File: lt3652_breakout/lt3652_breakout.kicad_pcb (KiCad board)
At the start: 2 copper layers, 45.2 x 33 mm, 15 parts, among them CON1 SLR PNL, P3 GND, U1 LT3652

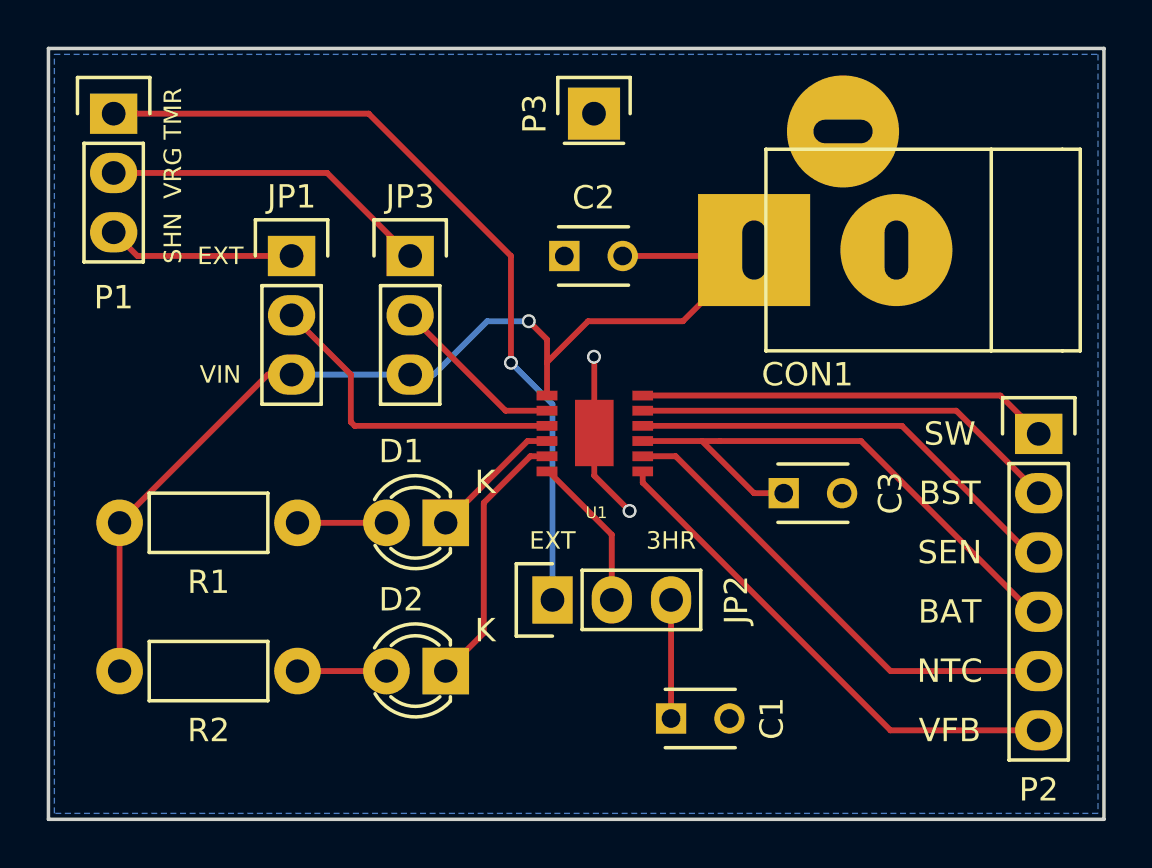
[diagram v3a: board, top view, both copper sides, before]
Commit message: Started work on Rev 0.2, with the aim of using trimmer to configure the LT3652
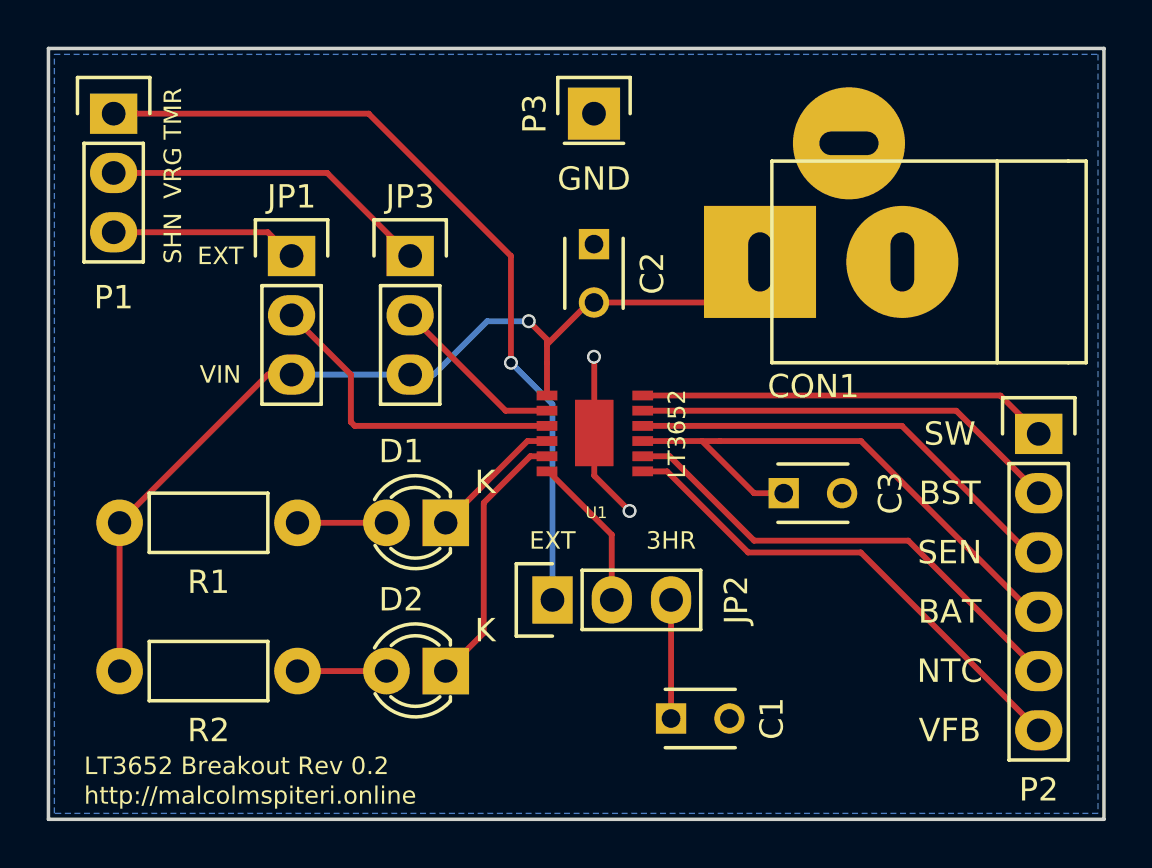
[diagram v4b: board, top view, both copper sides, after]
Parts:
- moved C2 1.37 mm to (147.3, 99.8), turned to 270 degrees
- moved CON1 0.57 mm to (160.5, 100.6)
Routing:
- net VIN: track 48.6 -> 45.1 mm
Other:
- board text added: "GND"
- board text added: "LT3652"
- board text added: "LT3652 Breakout Rev 0.2"
- board text added: "http://malcolmspiteri.online"
- board text removed: "Crappy LT3652 Breakout Board Rev 0.1 malcolmspiterionline@gmail.com"
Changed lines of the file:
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@@
     (area 123.876999 91.364999 169.239001 124.535001)
     (thickness 1.6)
-    (drawings 18)
-    (tracks 73)
+    (drawings 21)
+    (tracks 77)
     (zones 0)
     (modules 15)
@@
     (title "Crappy LT3652 Breakout")
     (date 2016-02-16)
-    (rev 0.1)
+    (rev 0.2)
     (company "Malcolm Spiteri")
   )
@@
     (aux_axis_origin 0 0)
     (grid_origin 147.066 107.95)
-    (visible_elements 7FFCFFFF)
+    (visible_elements 7FFFFFFF)
     (pcbplotparams
       (layerselection 0x010f0_80000001)
@@
   )
   (module Connect:JACK_ALIM (layer F.Cu)
-    (at 160.274 100.076 180)
+    (at 160.528 100.584 180)
     (descr "module 1 pin (ou trou mecanique de percage)")
     (tags "CONN JACK")
@@
   )
   (module Capacitors_ThroughHole:C_Disc_D3_P2.5 (layer F.Cu)
-    (at 146.05 100.33)
+    (at 147.32 99.822 270)
     (descr "Capacitor 3mm Disc, Pitch 2.5mm")
     (tags Capacitor)
-    (fp_text reference C2 (at 1.25 -2.5) (layer F.SilkS)
-      (effects (font (size 1 1) (thickness 0.15)))
-    )
-    (fp_text value 10uF (at 1.25 2.5) (layer F.Fab)
+    (fp_text reference C2 (at 1.25 -2.5 270) (layer F.SilkS)
+      (effects (font (size 1 1) (thickness 0.15)))
+    )
+    (fp_text value 10uF (at 1.25 2.5 270) (layer F.Fab)
       (effects (font (size 1 1) (thickness 0.15)))
     )
@@
     (fp_line (start -0.25 -1.25) (end 2.75 -1.25) (layer F.SilkS) (width 0.15))
     (fp_line (start 2.75 1.25) (end -0.25 1.25) (layer F.SilkS) (width 0.15))
-    (pad 1 thru_hole rect (at 0 0) (size 1.3 1.3) (drill 0.8) (layers *.Cu *.Mask F.SilkS)
+    (pad 1 thru_hole rect (at 0 0 270) (size 1.3 1.3) (drill 0.8) (layers *.Cu *.Mask F.SilkS)
       (net 13 GND))
-    (pad 2 thru_hole circle (at 2.5 0) (size 1.3 1.3) (drill 0.8001) (layers *.Cu *.Mask F.SilkS)
+    (pad 2 thru_hole circle (at 2.5 0 270) (size 1.3 1.3) (drill 0.8001) (layers *.Cu *.Mask F.SilkS)
       (net 7 VIN))
     (model Capacitors_ThroughHole.3dshapes/C_Disc_D3_P2.5.wrl
@@
     )
   )
+  (gr_text GND (at 147.32 97.028) (layer F.SilkS)
+    (effects (font (size 1 1) (thickness 0.2)))
+  )
+  (gr_text http://malcolmspiteri.online (at 125.476 123.444) (layer F.SilkS)
+    (effects (font (size 0.75 0.75) (thickness 0.15)) (justify left))
+  )
+  (gr_text "LT3652 Breakout Rev 0.2" (at 125.476 122.174) (layer F.SilkS)
+    (effects (font (size 0.75 0.75) (thickness 0.15)) (justify left))
+  )
+  (gr_text LT3652 (at 150.876 107.95 90) (layer F.SilkS)
+    (effects (font (size 0.75 0.75) (thickness 0.15)))
+  )
   (gr_text SHN (at 129.286 99.568 90) (layer F.SilkS)
     (effects (font (size 0.75 0.75) (thickness 0.15)))
@@
   (gr_text TMR (at 129.286 94.234 90) (layer F.SilkS)
     (effects (font (size 0.75 0.75) (thickness 0.15)))
-  )
-  (gr_text "Crappy LT3652 Breakout Board\nRev 0.1\nmalcolmspiterionline@gmail.com" (at 163.576 119.38) (layer B.SilkS)
-    (effects (font (size 1.5 1.5) (thickness 0.3)) (justify left mirror))
   )
   (gr_text VIN (at 131.318 105.41) (layer F.SilkS)
@@
   (segment (start 144.5925 108.9075) (end 142.6 110.9) (width 0.25) (layer F.Cu) (net 3))
   (segment (start 134.62 118.11) (end 138.43 118.11) (width 0.25) (layer F.Cu) (net 4))
-  (segment (start 134.366 100.33) (end 127.762 100.33) (width 0.25) (layer F.Cu) (net 5) (status 10))
-  (segment (start 127.762 100.33) (end 126.746 99.314) (width 0.25) (layer F.Cu) (net 5))
+  (segment (start 126.746 99.314) (end 133.35 99.314) (width 0.25) (layer F.Cu) (net 5) (status 400000))
+  (segment (start 133.35 99.314) (end 134.366 100.33) (width 0.25) (layer F.Cu) (net 5) (status 800000))
   (segment (start 145.3075 106.9575) (end 143.5335 106.9575) (width 0.25) (layer F.Cu) (net 6))
   (segment (start 143.5335 106.9575) (end 139.446 102.87) (width 0.25) (layer F.Cu) (net 6))
+  (segment (start 147.32 102.322) (end 152.694 102.322) (width 0.25) (layer F.Cu) (net 7) (status C00000))
+  (segment (start 152.694 102.322) (end 154.432 100.584) (width 0.25) (layer F.Cu) (net 7) (status C00000))
+  (segment (start 147.32 102.322) (end 147.106 102.322) (width 0.25) (layer F.Cu) (net 7) (status C00000))
+  (segment (start 147.106 102.322) (end 145.3075 104.1205) (width 0.25) (layer F.Cu) (net 7) (status 400000))
+  (segment (start 153.162 101.854) (end 154.432 100.584) (width 0.25) (layer F.Cu) (net 7))
+  (segment (start 154.178 100.33) (end 154.432 100.584) (width 0.25) (layer F.Cu) (net 7))
   (segment (start 127 118.11) (end 127 111.76) (width 0.25) (layer F.Cu) (net 7))
   (segment (start 134.366 105.41) (end 133.35 105.41) (width 0.25) (layer F.Cu) (net 7))
@@
   (segment (start 139.446 105.41) (end 140.462 105.41) (width 0.25) (layer B.Cu) (net 7))
   (segment (start 140.462 105.41) (end 142.748 103.124) (width 0.25) (layer B.Cu) (net 7))
-  (segment (start 145.3075 103.9055) (end 145.3075 104.902) (width 0.25) (layer F.Cu) (net 7))
+  (segment (start 145.3075 103.9055) (end 145.3075 104.1205) (width 0.25) (layer F.Cu) (net 7))
+  (segment (start 145.3075 104.1205) (end 145.3075 104.902) (width 0.25) (layer F.Cu) (net 7))
   (segment (start 144.526 103.124) (end 145.3075 103.9055) (width 0.25) (layer F.Cu) (net 7))
   (via (at 144.526 103.124) (size 0.6) (drill 0.4) (layers F.Cu B.Cu) (net 7))
@@
   (segment (start 127 111.76) (end 127 110.998) (width 0.25) (layer F.Cu) (net 7))
   (segment (start 134.366 105.41) (end 139.446 105.41) (width 0.25) (layer B.Cu) (net 7) (status 10))
-  (segment (start 148.55 100.33) (end 153.924 100.33) (width 0.25) (layer F.Cu) (net 7))
-  (segment (start 153.924 100.33) (end 154.178 100.076) (width 0.25) (layer F.Cu) (net 7))
+  (segment (start 154.178 100.838) (end 154.432 100.584) (width 0.25) (layer F.Cu) (net 7) (status 30))
   (segment (start 145.3075 106.3075) (end 145.3075 104.902) (width 0.25) (layer F.Cu) (net 7))
-  (segment (start 145.3075 104.902) (end 145.3075 104.8825) (width 0.25) (layer F.Cu) (net 7))
-  (segment (start 151.13 103.124) (end 154.178 100.076) (width 0.25) (layer F.Cu) (net 7))
-  (segment (start 147.066 103.124) (end 151.13 103.124) (width 0.25) (layer F.Cu) (net 7))
-  (segment (start 145.3075 104.8825) (end 147.066 103.124) (width 0.25) (layer F.Cu) (net 7))
-  (segment (start 153.924 100.33) (end 153.924 100.05568) (width 0.25) (layer F.Cu) (net 7))
+  (segment (start 154.178 100.838) (end 154.178 100.56368) (width 0.25) (layer F.Cu) (net 7) (status 30))
   (segment (start 126.746 94.234) (end 137.668 94.234) (width 0.25) (layer F.Cu) (net 8))
   (segment (start 145.542 106.68) (end 145.542 115.062) (width 0.25) (layer B.Cu) (net 8))
@@
   (segment (start 165.93 113.03) (end 160.5075 107.6075) (width 0.25) (layer F.Cu) (net 18))
   (segment (start 160.5075 107.6075) (end 149.4075 107.6075) (width 0.25) (layer F.Cu) (net 18))
-  (segment (start 149.4075 108.9075) (end 150.8175 108.9075) (width 0.25) (layer F.Cu) (net 19))
-  (segment (start 160.02 118.11) (end 166.37 118.11) (width 0.25) (layer F.Cu) (net 19))
-  (segment (start 150.8175 108.9075) (end 160.02 118.11) (width 0.25) (layer F.Cu) (net 19))
-  (segment (start 149.4075 109.5575) (end 149.4075 110.0375) (width 0.25) (layer F.Cu) (net 20))
-  (segment (start 160.02 120.65) (end 166.37 120.65) (width 0.25) (layer F.Cu) (net 20))
-  (segment (start 149.4075 110.0375) (end 160.02 120.65) (width 0.25) (layer F.Cu) (net 20))
+  (segment (start 149.4075 108.9075) (end 150.5635 108.9075) (width 0.25) (layer F.Cu) (net 19))
+  (segment (start 160.782 112.522) (end 166.37 118.11) (width 0.25) (layer F.Cu) (net 19))
+  (segment (start 154.178 112.522) (end 160.782 112.522) (width 0.25) (layer F.Cu) (net 19))
+  (segment (start 150.5635 108.9075) (end 154.178 112.522) (width 0.25) (layer F.Cu) (net 19))
+  (segment (start 149.4075 109.5575) (end 150.4515 109.5575) (width 0.25) (layer F.Cu) (net 20))
+  (segment (start 158.75 113.03) (end 166.37 120.65) (width 0.25) (layer F.Cu) (net 20))
+  (segment (start 153.924 113.03) (end 158.75 113.03) (width 0.25) (layer F.Cu) (net 20))
+  (segment (start 150.4515 109.5575) (end 153.924 113.03) (width 0.25) (layer F.Cu) (net 20))
   (zone (net 13) (net_name GND) (layer B.Cu) (hatch edge 0.508)
     (connect_pads (clearance 0.508))

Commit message: WIP on Rev 0.2
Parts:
- removed JP1: SHDN OPT, Pin_Headers:Pin_Header_Straight_1x03
- removed JP3: VREG OPT, Pin_Headers:Pin_Header_Straight_1x03
- removed P2: , Pin_Headers:Pin_Header_Straight_1x06
- removed P3: GND, Pin_Headers:Pin_Header_Straight_1x01
- added RV1: POT, bourns_trim_pots:Bourns_3362P_Trimmer, F.Cu at (166.1, 120.8)
- added RV2: POT, bourns_trim_pots:Bourns_3362P_Trimmer, F.Cu at (166.1, 113.8)
- added W1: TEST_1P, pcb_test_points:KEYSTONE_5016_PCB_Test_Point, F.Cu at (177.1, 114.5)
- added W2: TEST_1P, pcb_test_points:KEYSTONE_5016_PCB_Test_Point, F.Cu at (177.0, 120.5)
- C1, C2, C3: footprint Capacitors_ThroughHole:C_Disc_D3_P2.5 -> Capacitors_SMD:C_0603_HandSoldering
- D1: value (none) -> 3mm GRN; footprint LEDs:LED-3MM -> LEDs:LED_0603
- D2: value (none) -> 3mm RED; footprint LEDs:LED-3MM -> LEDs:LED_0603
- P1: value (none) -> CONN_01X09; footprint Pin_Headers:Pin_Header_Straight_1x03 -> Pin_Headers:Pin_Header_Straight_1x09
- R1, R2: footprint Resistors_ThroughHole:Resistor_Horizontal_RM7mm -> Resistors_SMD:R_0603_HandSoldering
- moved P1 52.4 mm to (167.9, 126.7), turned to 270 degrees
- moved C2 17.3 mm to (160.4, 111.2), turned to 180 degrees
- moved R2 15.7 mm to (147.3, 108.8), turned to 90 degrees
- moved R1 15.0 mm to (149.3, 108.8), turned to 90 degrees
- moved U1 13.2 mm to (157.9, 116.0), turned to 270 degrees
- moved D2 13.1 mm to (152.7, 112.2)
- moved D1 11.8 mm to (152.7, 110.0)
- moved C3 10.9 mm to (157.6, 121.2), turned to 270 degrees
- moved JP2 8.14 mm to (147.6, 123.0), turned to 180 degrees
- moved C1 6.41 mm to (147.7, 114.5)
- moved CON1 5.17 mm to (161.6, 105.7)
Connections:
- C2 pad 2: VIN -> /VIN
- CON1 pad 1: VIN -> /VIN
- CON1 pad 3: Net-(CON1-Pad3) -> (no net)
- P1 pad 1: Net-(JP2-Pad1) -> /VIN
- P1 pad 2: Net-(JP3-Pad1) -> Net-(P1-Pad2)
- P1 pad 3: Net-(JP1-Pad1) -> Net-(P1-Pad3)
- R1 pad 2: VIN -> /VIN
- R2 pad 2: VIN -> /VIN
- U1 pad 1: VIN -> /VIN
- U1 pad 10: Net-(P2-Pad3) -> Net-(P1-Pad4)
- U1 pad 11: Net-(P2-Pad2) -> Net-(P1-Pad3)
- U1 pad 12: Net-(P2-Pad1) -> Net-(P1-Pad2)
- U1 pad 2: VREG -> /VIN_REG
- U1 pad 3: SHDN -> /SHDN
- U1 pad 7: Net-(P2-Pad6) -> Net-(P1-Pad7)
- U1 pad 8: Net-(P2-Pad5) -> Net-(P1-Pad6)
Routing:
- net VIN: track 45.1 -> 0.00 mm, vias 1 -> 0
- net /VIN: track 0.00 -> 42.7 mm, vias 0 -> 2
- net Net-(JP2-Pad1): track 35.0 -> 4.74 mm, vias 1 -> 0
- net Net-(P2-Pad6): track 21.6 -> 0.00 mm
- net Net-(P2-Pad5): track 20.8 -> 0.00 mm
- net Net-(P2-Pad3): track 19.2 -> 0.00 mm
- net Net-(P2-Pad2): track 18.4 -> 0.00 mm
- net Net-(P2-Pad1): track 17.6 -> 0.00 mm
- net /VIN_REG: track 0.00 -> 16.2 mm
- net Net-(C3-Pad1): track 24.4 -> 9.75 mm
- net Net-(JP3-Pad1): track 14.2 -> 0.00 mm
- net SHDN: track 14.1 -> 0.00 mm
- net /SHDN: track 0.00 -> 12.1 mm
- net Net-(P1-Pad2): track 0.00 -> 11.0 mm
- net Net-(P1-Pad3): track 0.00 -> 10.2 mm
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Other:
- board size 45.2 x 33 mm -> 24.2 x 32.2 mm
- board text added: "BOOST"
- board text removed: "BAT"
- board text removed: "BST"
- board text removed: "LT3652"
- board text removed: "NTC"
- board text removed: "SEN"
- board text removed: "SHN"
- board text removed: "TMR"
- board text removed: "VFB"
- board text removed: "VRG"
- board text removed: "http://malcolmspiteri.online"

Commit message: WIP on Rev 0.2
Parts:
- removed C2: 10uF, Capacitors_SMD:C_0603_HandSoldering
- removed P1: CONN_01X09, Pin_Headers:Pin_Header_Straight_1x09
- removed W1, W2: TEST_1P, pcb_test_points:KEYSTONE_5016_PCB_Test_Point
- added Cbat1: 100uF, Capacitors_ThroughHole:C_Radial_D5_L6_P2.5, F.Cu at (155.9, 103.8)
- added Cbs1: 1uF, Capacitors_SMD:C_0603_HandSoldering, F.Cu at (144.6, 96.0)
- added Cvfbat1: 20pF, Capacitors_SMD:C_0603_HandSoldering, F.Cu at (144.6, 100.2)
- added Cvin2: 10uF, Capacitors_SMD:C_0603_HandSoldering, F.Cu at (133.0, 95.8)
- added Dbatbst1: D_Small, Diodes_ThroughHole:Diode_DO-35_SOD27_Horizontal_RM10, F.Cu at (149.4, 99.7)
- added Dflybk1: ZLLS500, diodes:DIODES_INC_ZLLS500, F.Cu at (139.8, 93.8)
- added Dvin1: D_Schottky_Small_ZLLS500, diodes:DIODES_INC_ZLLS500, F.Cu at (136.0, 93.8)
- added JP1: TIMER OPT, Pin_Headers:Pin_Header_Straight_1x03, F.Cu at (136.6, 106.5)
- added JP3: JUMPER3, Pin_Headers:Pin_Header_Straight_1x03, F.Cu at (127.9, 101.3)
- added Lsw1: 10uH, inductors:PANASONIC_ELC09D100F, F.Cu at (145.5, 86.2)
- added Pbat1: JST PH, w_conn_jst-ph:b2b-ph-kl, F.Cu at (155.7, 108.7)
- added Pled1: CONN_01X03, Pin_Headers:Pin_Header_Straight_1x03, F.Cu at (118.3, 106.5)
- added Pload1: JST PH, w_conn_jst-ph:b2b-ph-kl, F.Cu at (163.5, 100.8)
- added Pload2: USB_A, connectors:WURTH_ELEKTRONIK_629104151021, F.Cu at (157.9, 89.2)
- added REF** (x2): MHH-20_ABS_Plastic_Box, MHH-20_ABS_Plastic_Box, F.Cu at (0.00, 0.00)
- added Rfb1: 90k, Resistors_SMD:R_0603_HandSoldering, F.Cu at (140.3, 107.5)
- added Rfb2: 330k, Resistors_SMD:R_0603_HandSoldering, F.Cu at (141.4, 103.8)
- added Rfb3: 179k, Resistors_SMD:R_0603_HandSoldering, F.Cu at (139.3, 103.8)
- added Rsense1: 250mO, Resistors_SMD:R_0603_HandSoldering, F.Cu at (145.4, 93.5)
- added Wbat1: TEST_1P, pcb_test_points:HARWIN_S1751-46, F.Cu at (144.6, 105.3)
- added Wgnd1: TEST_1P, pcb_test_points:HARWIN_S1751-46, F.Cu at (135.4, 110.7)
- added Wshdn1: TEST_1P, pcb_test_points:HARWIN_S1751-46, F.Cu at (125.6, 95.8)
- added Wsw1: TEST_1P, pcb_test_points:HARWIN_S1751-46, F.Cu at (149.1, 102.5)
- added Wvfb1: TEST_1P, pcb_test_points:HARWIN_S1751-46, F.Cu at (149.1, 105.3)
- added Wvreg1: TEST_1P, pcb_test_points:HARWIN_S1751-46, F.Cu at (128.8, 95.8)
- C1: value 0.68uF -> C_Small
- JP2: value TIMER OPT -> JUMPER3
- moved RV2 49.6 mm to (120.0, 95.3), turned to 90 degrees
- moved RV1 46.1 mm to (136.9, 85.0), turned to 0 degrees
- moved CON1 42.3 mm to (124.2, 85.8), turned to 0 degrees
- moved U1 25.8 mm to (138.7, 98.8), turned to 0 degrees
- moved JP2 25.7 mm to (127.9, 106.5), turned to 270 degrees
- moved C3 22.7 mm to (144.6, 102.5), turned to 0 degrees
- moved D1 20.2 mm to (133.0, 114.5), turned to 0 degrees
- moved C1 19.3 mm to (132.7, 102.2), turned to 180 degrees
- moved R1 19.2 mm to (132.9, 98.8), turned to 180 degrees
- moved R2 16.6 mm to (132.9, 100.5), turned to 180 degrees
- moved D2 15.2 mm to (137.7, 114.5)
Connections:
- net Net-(C3-Pad1) renamed /BAT
- CON1 pad 1: /VIN -> Net-(CON1-Pad1)
- D1 pad 2: Net-(D1-Pad2) -> GND
- D2 pad 2: Net-(D2-Pad2) -> GND
- JP2 pad 1: Net-(JP2-Pad1) -> Net-(D2-Pad1)
- JP2 pad 2: TIMER -> Net-(JP2-Pad2)
- JP2 pad 3: Net-(C1-Pad1) -> Net-(JP2-Pad3)
- R1 pad 1: Net-(D1-Pad2) -> Net-(R1-Pad1)
- R1 pad 2: /VIN -> Net-(JP3-Pad2)
- R2 pad 1: Net-(D2-Pad2) -> Net-(R2-Pad1)
- R2 pad 2: /VIN -> Net-(JP2-Pad2)
- RV1 pad 1: /VIN -> Net-(CON1-Pad1)
- RV2 pad 1: /VIN -> Net-(CON1-Pad1)
- U1 pad 10: Net-(P1-Pad4) -> /SENSE
- U1 pad 11: Net-(P1-Pad3) -> /BOOST
- U1 pad 12: Net-(P1-Pad2) -> /SW
- U1 pad 4: Net-(D1-Pad1) -> Net-(R1-Pad1)
- U1 pad 5: Net-(D2-Pad1) -> Net-(R2-Pad1)
- U1 pad 6: TIMER -> Net-(JP1-Pad2)
- U1 pad 7: Net-(P1-Pad7) -> /VFB
- U1 pad 8: Net-(P1-Pad6) -> (no net)
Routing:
- net /VIN: track 42.7 -> 5.11 mm, vias 2 -> 0
- net /SENSE: track 0.00 -> 24.8 mm, vias 0 -> 3
- net Net-(CON1-Pad1): track 0.00 -> 19.5 mm
- net /VFB: track 0.00 -> 16.2 mm, vias 0 -> 2
- net /SW: track 0.00 -> 16.1 mm
- net TIMER: track 11.4 -> 0.00 mm
- net Net-(P1-Pad2): track 11.0 -> 0.00 mm
- net Net-(P1-Pad3): track 10.2 -> 0.00 mm
- net Net-(P1-Pad7): track 10.1 -> 0.00 mm
- net Net-(P1-Pad4): track 9.46 -> 0.00 mm
- net Net-(P1-Pad6): track 9.33 -> 0.00 mm
- net /VIN_REG: track 16.2 -> 25.4 mm
- net /BAT: track 9.75 -> 18.8 mm
- net Net-(D1-Pad1): track 6.44 -> 0.00 mm
- net Net-(D2-Pad2): track 5.60 -> 0.00 mm
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- removed copper zone on B.Cu, net GND
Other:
- board outline removed
- board text removed: "3HR"
- board text removed: "BOOST"
- board text removed: "EXT"
- board text removed: "GND"
- board text removed: "SW"
- board text removed: "VIN"
